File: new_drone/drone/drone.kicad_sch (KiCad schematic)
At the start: 29 parts, among them J1 Conn_01x06, SW1 SW_Push_Open, SW2 SW_Push_Open, U1 ESP32-WROOM-32, U2 MPU-6050, U4 BMP280, U5 MCP8063, U5 TPS63001, U6 MCP8063, U7 MCP8063, U8 MCP8063

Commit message: first wiring
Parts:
- removed C4, C5, C7: 0.1uF, Capacitor_SMD:C_0603_1608Metric, symbol Device:C
- removed L1: LPS4012-103MRB, LPS4012:IND_LPS4012-103MRB, symbol LPS4012:LPS4012-103MRB
- removed R11: 100, Resistor_SMD:R_0603_1608Metric, symbol Device:R_Small
- removed U5: TPS63001, Package_SON:Texas_DRC0010J_ThermalVias, symbol Regulator_Switching:TPS63000
- removed U6, U7, U8: MCP8063, Package_DFN_QFN:DFN-8-1EP_4x4mm_P0.8mm_EP2.5x3.6mm, symbol MCP8063:MCP8063
- added C1 (x3): C, Capacitor_SMD:C_0603_1608Metric, symbol Device:C
- added TP1, TP2, TP3: TestPoint, TestPoint:TestPoint_Pad_3.0x3.0mm, symbol Connector:TestPoint
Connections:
- net GND: now also U5.5 (GND), U5.9 (GND), C1.2, C1.2, C1.2
- net MOTOR_1: now also U5.8 (PWM)
- net at U5.2 (Vbias): now also C1.1
- net at U5.3 (OUT1): now also TP2.1
- net at U5.4 (OUT2): now also TP3.1
- net at U5.6 (OUT3): now also TP1.1
- net +BATT: now reaches U5.7 (VDD)
- net +BATT: now also C1.1, C1.1

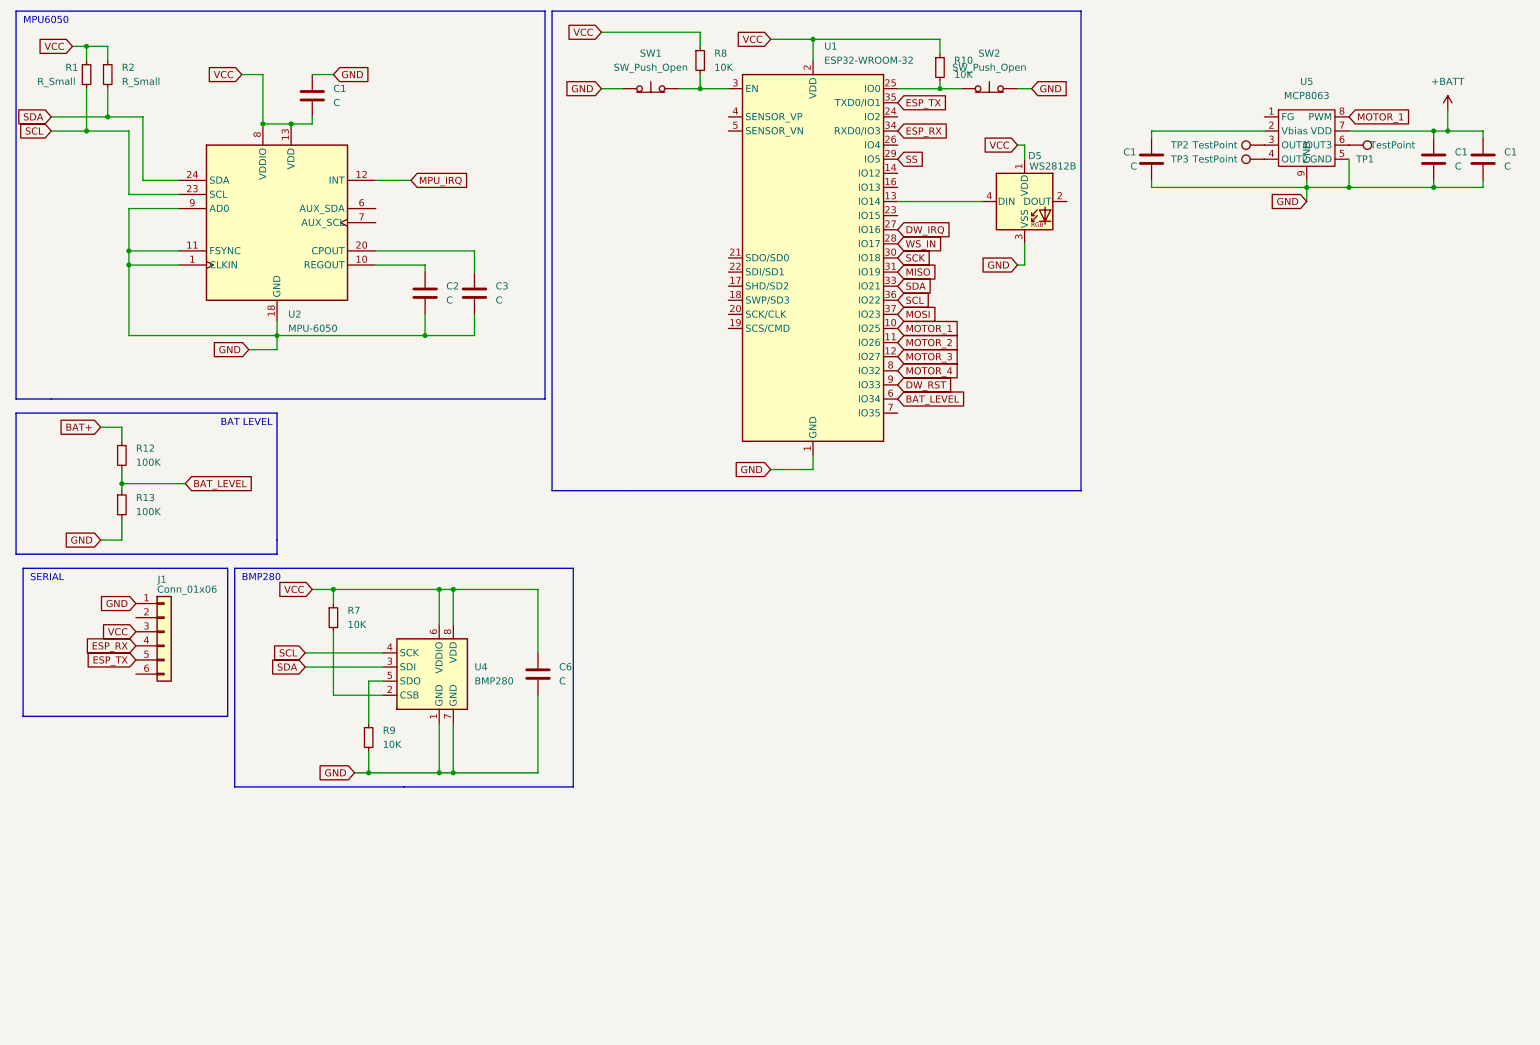
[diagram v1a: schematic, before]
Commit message: add all ESC
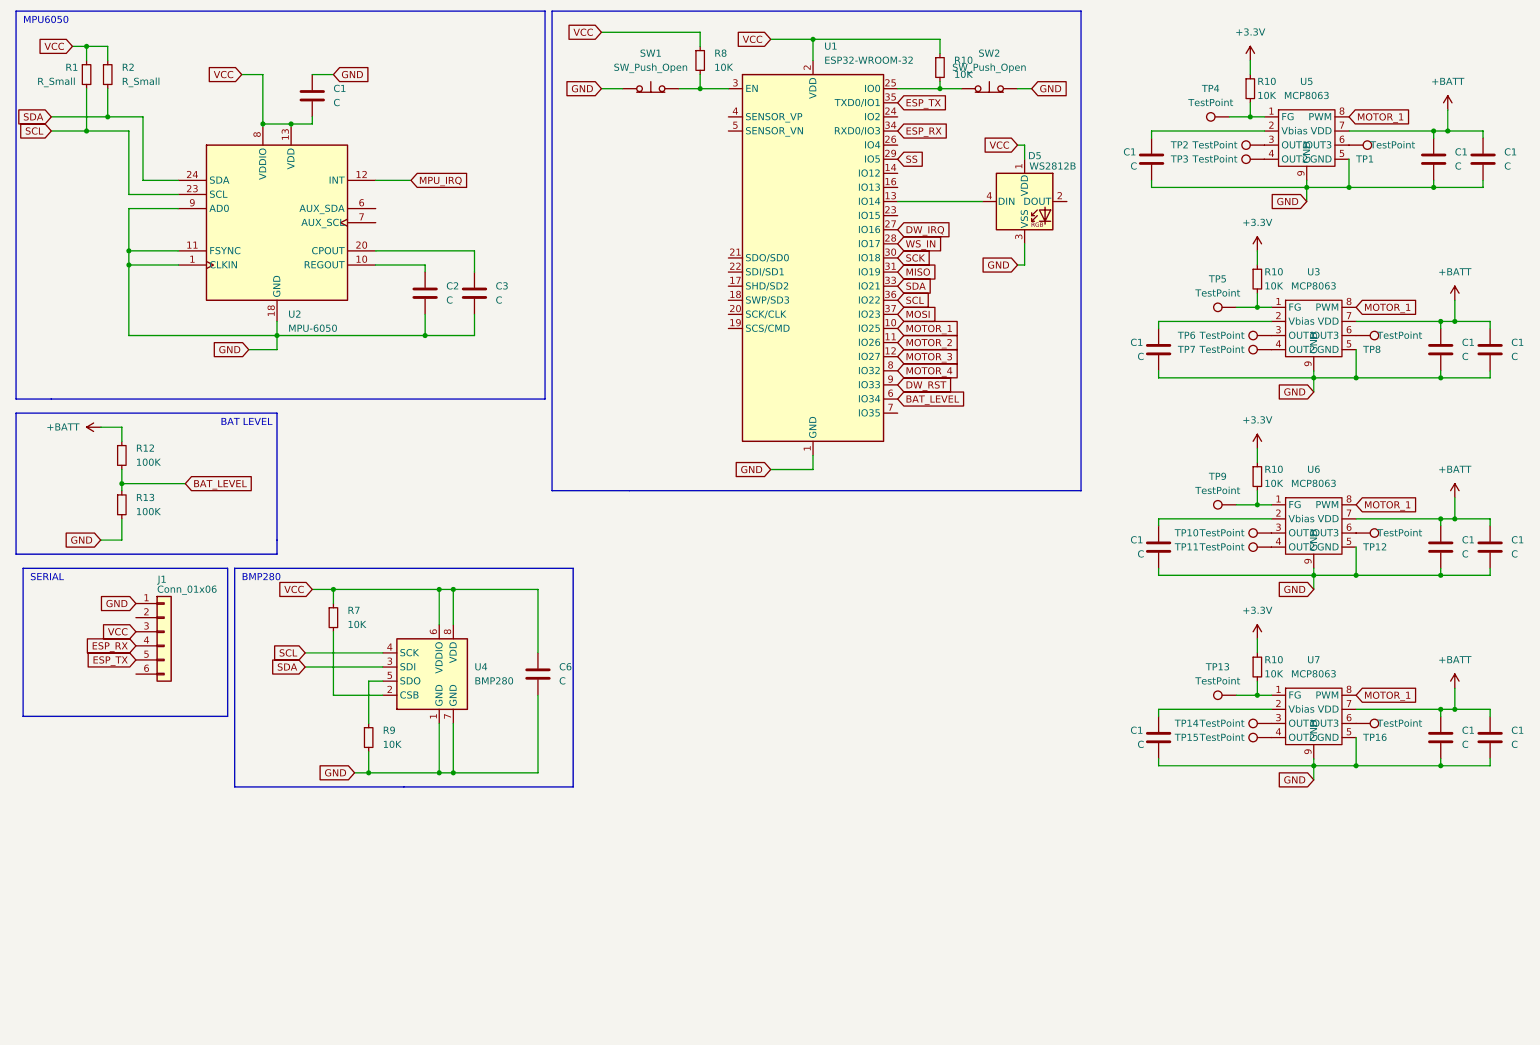
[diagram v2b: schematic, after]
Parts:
- added C1 (x9): C, Capacitor_SMD:C_0603_1608Metric, symbol Device:C
- added R10 (x4): 10K, Resistor_SMD:R_0603_1608Metric, symbol Device:R_Small
- added TP10, TP11, TP12, TP14, TP15, TP16, TP6, TP7, TP8: TestPoint, TestPoint:TestPoint_Pad_3.0x3.0mm, symbol Connector:TestPoint
- added TP13, TP4, TP5, TP9: TestPoint, TestPoint:TestPoint_Pad_1.0x1.0mm, symbol Connector:TestPoint
- added U3, U6, U7: MCP8063, Package_DFN_QFN:DFN-8-1EP_4x4mm_P0.8mm_EP2.5x3.6mm, symbol MCP8063:MCP8063
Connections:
- net BAT+ is gone; now on net +BATT: R12.1
- net +BATT: now also C1.1, C1.1, C1.1, C1.1, C1.1, C1.1, U3.7 (VDD), U6.7 (VDD), U7.7 (VDD)
- net GND: now also C1.2, C1.2, C1.2, C1.2, C1.2, C1.2, C1.2, C1.2, C1.2, U3.5 (GND), U3.9 (GND), U6.5 (GND), U6.9 (GND), U7.5 (GND), U7.9 (GND)
- net MOTOR_1: now also U3.8 (PWM), U6.8 (PWM), U7.8 (PWM)
- net at U5.1 (FG): now also R10.2, TP4.1
- new net: R10.2, TP9.1, U6.1 (FG)
- new net: C1.1, U7.2 (Vbias)
- new net: R10.2, TP5.1, U3.1 (FG)
- new net: C1.1, U6.2 (Vbias)
- new net: TP14.1, U7.3 (OUT1)
- new net: TP7.1, U3.4 (OUT2)
- new net: C1.1, U3.2 (Vbias)
- new net: TP6.1, U3.3 (OUT1)
- new net: TP8.1, U3.6 (OUT3)
- new net: TP16.1, U7.6 (OUT3)
- new net: TP15.1, U7.4 (OUT2)
- new net: TP10.1, U6.3 (OUT1)
- new net: TP11.1, U6.4 (OUT2)
- new net: TP12.1, U6.6 (OUT3)
- new net: R10.2, TP13.1, U7.1 (FG)
- new net +3.3V: R10.1, R10.1, R10.1, R10.1

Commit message: add regulator
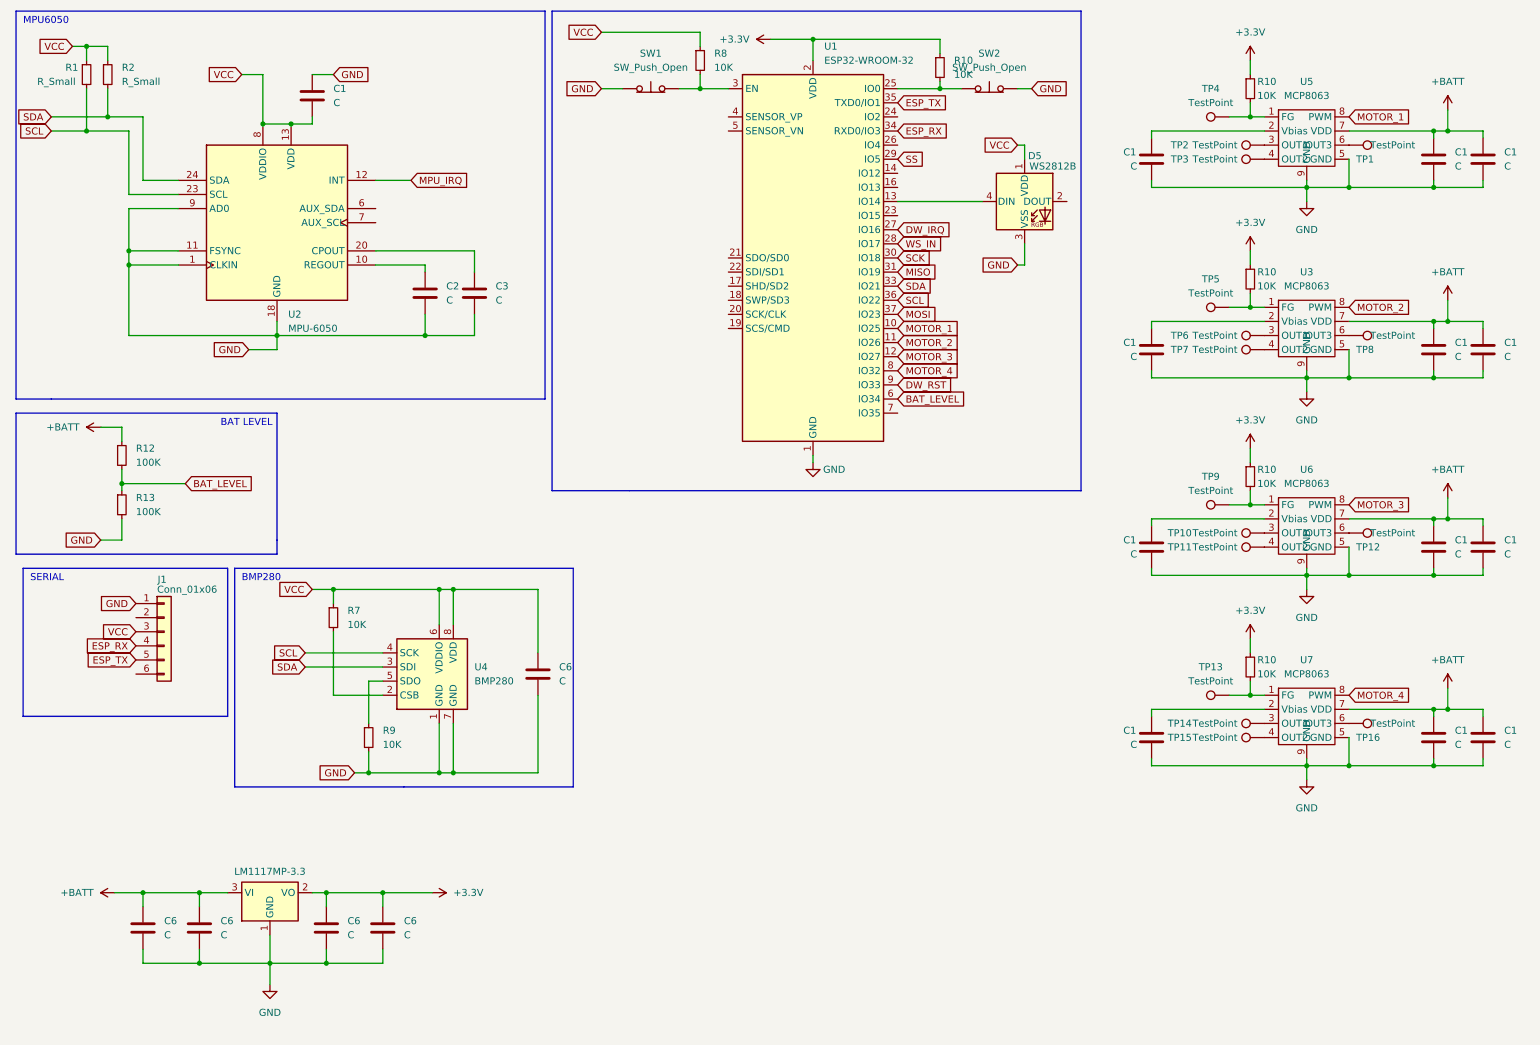
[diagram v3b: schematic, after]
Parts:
- added C6 (x4): C, Capacitor_SMD:C_0603_1608Metric, symbol Device:C
- added U9: LM1117MP-3.3, Package_TO_SOT_SMD:SOT-223-3_TabPin2, symbol Regulator_Linear:LM1117MP-3.3
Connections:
- net +3.3V: now also R10.1, U1.2 (VDD), C6.1, C6.1, U9.2 (VO)
- net +BATT: now also C6.1, C6.1, U9.3 (VI)
- net GND: now also C6.2, C6.2, C6.2, C6.2, U9.1 (GND)
- net MOTOR_1: no longer U3.8 (PWM), U6.8 (PWM), U7.8 (PWM)
- net MOTOR_2: now also U3.8 (PWM)
- net MOTOR_3: now also U6.8 (PWM)
- net MOTOR_4: now also U7.8 (PWM)
- net VCC: no longer R10.1, U1.2 (VDD)
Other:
- moved on the sheet: C1, R10, TP10, TP11, TP12, TP13, TP14, TP15, TP16, TP5, TP6, TP7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

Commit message: add regulator + xt60 connector
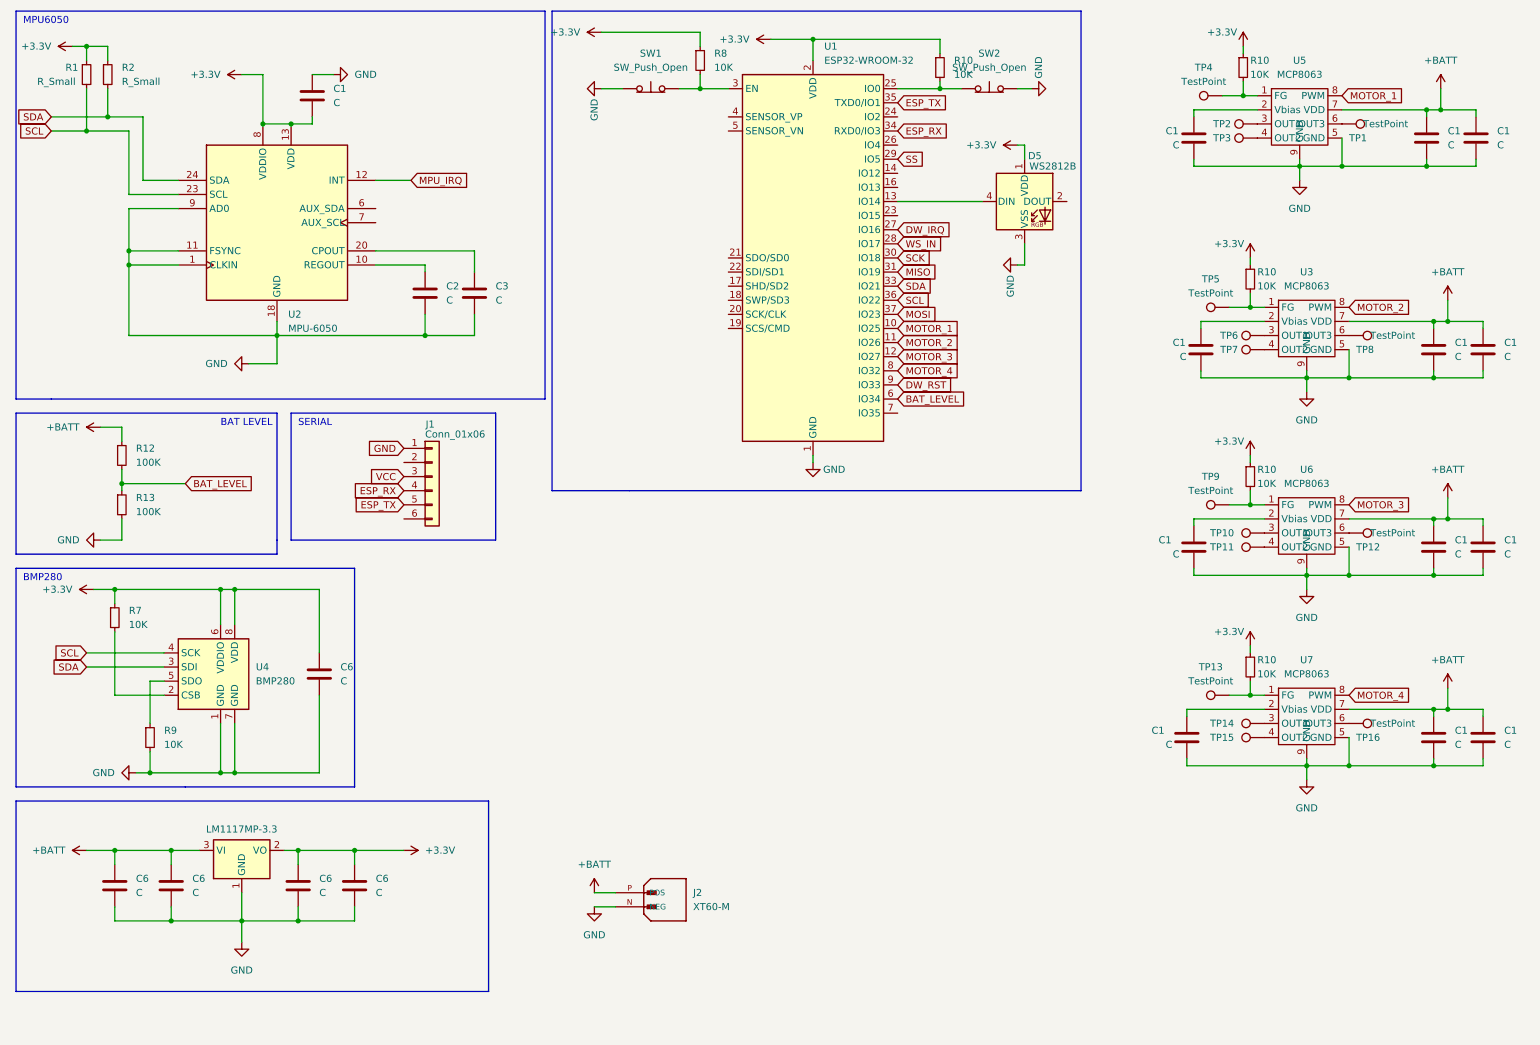
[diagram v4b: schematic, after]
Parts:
- added J2: XT60-M, Connector_AMASS:AMASS_XT60-M_1x02_P7.20mm_Vertical, symbol XT60:XT60-M
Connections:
- net +3.3V: now also C1.2, C6.1, D5.1 (VDD), R1.1, R2.1, R7.1, R8.1, U2.13 (VDD), U2.8 (VDDIO), U4.6 (VDDIO), U4.8 (VDD)
- net +BATT: now also J2.P (POS)
- net GND: now also J2.N (NEG)
- net VCC: no longer C1.2, C6.1, D5.1 (VDD), R1.1, R2.1, R7.1, R8.1, U2.13 (VDD), U2.8 (VDDIO), U4.6 (VDDIO), U4.8 (VDD)
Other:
- moved on the sheet: C1, C6, J1, R10, R7, R9, TP1, TP2, TP3, TP4, U4, U5
